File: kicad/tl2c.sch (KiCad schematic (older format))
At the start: 31 parts, among them IC101 ATTINY20-X, P101 12VDC, P102 I2C Master, P103 Spare, P104 ISP Header, P105 LED_DRIVER, P106 240VAC, P107 LED_DRIVER, P108 LED_OUT, SW101 TL3315NF160Q

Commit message: Revamped the master pcb layout for the mounting holes and the actual footprint for the terminal blocks
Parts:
- P102: footprint Pin_Headers:Pin_Header_Straight_1x03 -> tl2c-footprint:Spring_Terminal_Block_1_x_3
- P106: footprint tl2c-footprint:Pin_Header_1_x_2_5mmPitch -> tl2c-footprint:Spring_Terminal_Block_1_x_2_5mm
- P108: footprint tl2c-footprint:Pin_Header_1_x_6_54mmPitch -> tl2c-footprint:Spring_Terminal_Block_1_x_6_5mm; Conrad-PN (none) -> Value; Digikey-PN (none) -> Value; MFP (none) -> Value
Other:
- note added: "Should a PTC be considered?"
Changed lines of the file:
@@
 F 0 "P102" H 2100 3250 50  0000 C CNN
 F 1 "I2C Master" V 2200 3050 50  0000 C CNN
-F 2 "Pin_Headers:Pin_Header_Straight_1x03" H 2100 3050 50  0001 C CNN
+F 2 "tl2c-footprint:Spring_Terminal_Block_1_x_3" H 2100 3050 50  0001 C CNN
 F 3 "" H 2100 3050 50  0000 C CNN
 F 4 "Value" H 2100 3050 60  0001 C CNN "MFP"
@@
 F 0 "P106" H 6950 1350 50  0000 C CNN
 F 1 "240VAC" V 7050 1200 50  0000 C CNN
-F 2 "tl2c-footprint:Pin_Header_1_x_2_5mmPitch" H 6950 1200 50  0001 C CNN
+F 2 "tl2c-footprint:Spring_Terminal_Block_1_x_2_5mm" H 6950 1200 50  0001 C CNN
 F 3 "" H 6950 1200 50  0000 C CNN
 F 4 "Value" H 6950 1200 60  0001 C CNN "MFP"
@@
 F 0 "P108" H 9950 1750 50  0000 C CNN
 F 1 "LED_OUT" V 10050 1400 50  0000 C CNN
-F 2 "tl2c-footprint:Pin_Header_1_x_6_54mmPitch" H 9950 1400 50  0001 C CNN
+F 2 "tl2c-footprint:Spring_Terminal_Block_1_x_6_5mm" H 9950 1400 50  0001 C CNN
 F 3 "" H 9950 1400 50  0000 C CNN
+F 4 "Value" H 9950 1400 60  0001 C CNN "MFP"
+F 5 "Value" H 9950 1400 60  0001 C CNN "Conrad-PN"
+F 6 "Value" H 9950 1400 60  0001 C CNN "Digikey-PN"
 	1    9950 1400
 	1    0    0    -1
@@
 Text Notes 6850 4150 0    60   ~ 0
 TODO - Change the relay to  AZ7705T-1A-12DEF - Conrad.\nor FIN 43.41.7 12V - Reichelt
+Text Notes 6950 2450 0    60   ~ 0
+Should a PTC be considered?
 $EndSCHEMATC

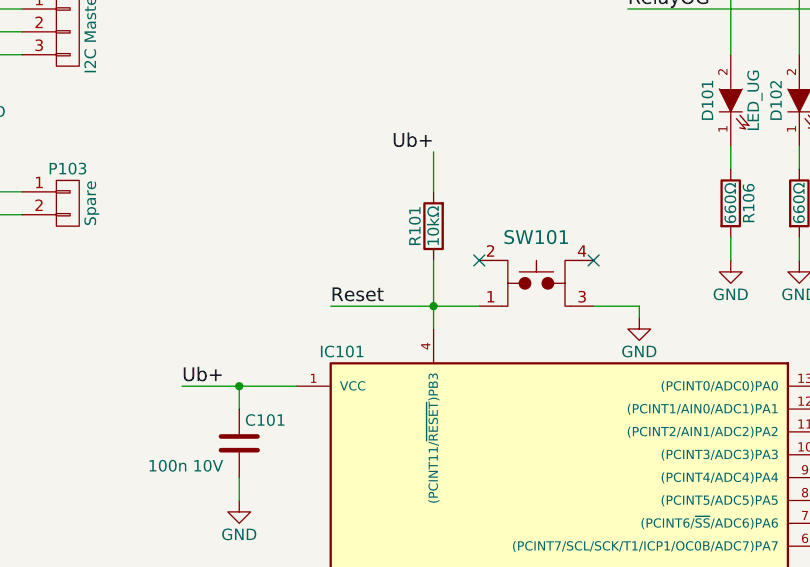
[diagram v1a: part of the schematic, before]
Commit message: Fixed junction on three wires instead of two, two wire connections. Added first look at the Gerbers
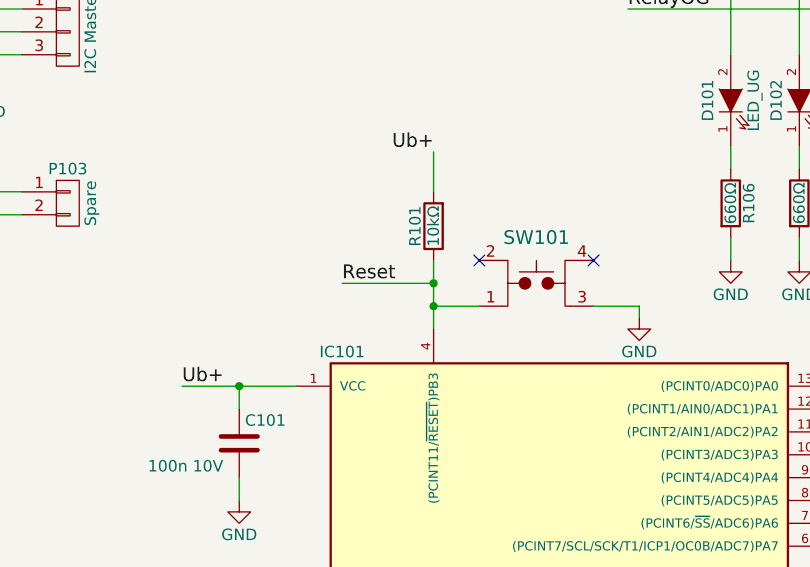
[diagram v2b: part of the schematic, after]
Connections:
- wire segments 97 -> 98
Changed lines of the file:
@@
 Wire Wire Line
 	3700 4050 3700 4350
-Wire Wire Line
-	3250 4250 3900 4250
-Connection ~ 3700 4250
-Text Label 3250 4250 0    60   ~ 0
+Text Label 3300 4150 0    60   ~ 0
 Reset
 NoConn ~ 3900 4050
@@
 Text Notes 6950 2450 0    60   ~ 0
 Should a PTC be considered?
+Wire Wire Line
+	3300 4150 3700 4150
+Connection ~ 3700 4150
+Wire Wire Line
+	3900 4250 3700 4250
+Connection ~ 3700 4250
 $EndSCHEMATC

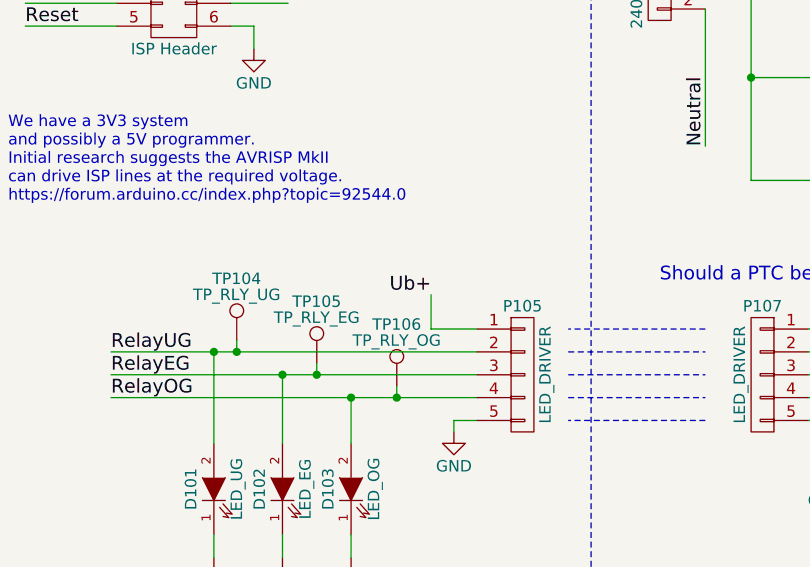
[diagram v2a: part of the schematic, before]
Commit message: Corrected the Ub+ to the LV board... should be U+
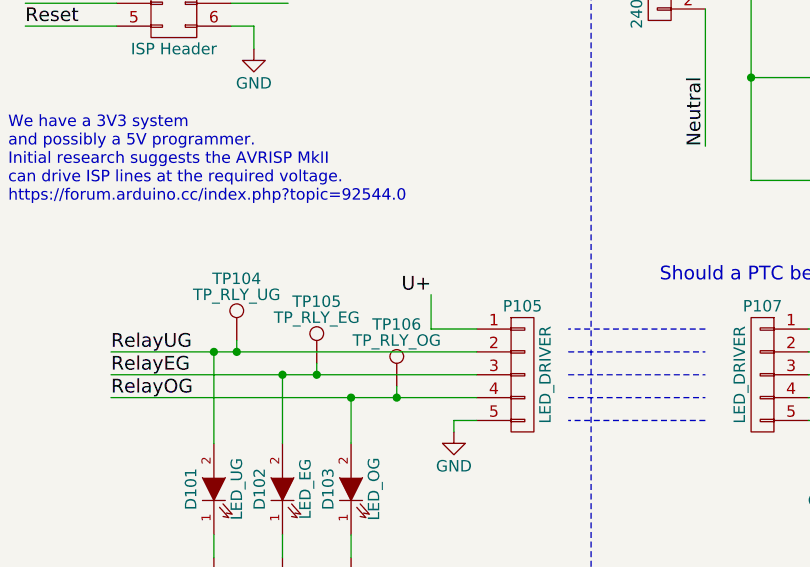
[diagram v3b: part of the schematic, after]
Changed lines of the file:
@@
 Wire Wire Line
 	5950 2650 5950 2500
-Text Label 5950 2500 2    60   ~ 0
-Ub+
 $Comp
 L CONN_01X05 P105
@@
 	3900 4250 3700 4250
 Connection ~ 3700 4250
+Text Label 5950 2500 2    60   ~ 0
+U+
 $EndSCHEMATC

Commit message: More rework on the board for the correct terminal blocks and case
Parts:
- removed P106: 240VAC, tl2c-footprint:Spring_Terminal_Block_1_x_2_5mm, symbol CONN_01X02
- removed P108: LED_OUT, tl2c-footprint:Spring_Terminal_Block_1_x_6_5mm, symbol CONN_01X06
- added P106: 240VAC, tl2c-footprint:Spring_Terminal_Block_1_x_2_5mm, symbol Term_01X02
- added P108: LED_OUT, tl2c-footprint:Spring_Terminal_Block_1_x_6_5mm, symbol TerminalBlock_1x6
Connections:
- wire segments 98 -> 107
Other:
- moved on the sheet: P107, REL101B, REL102B, REL103B

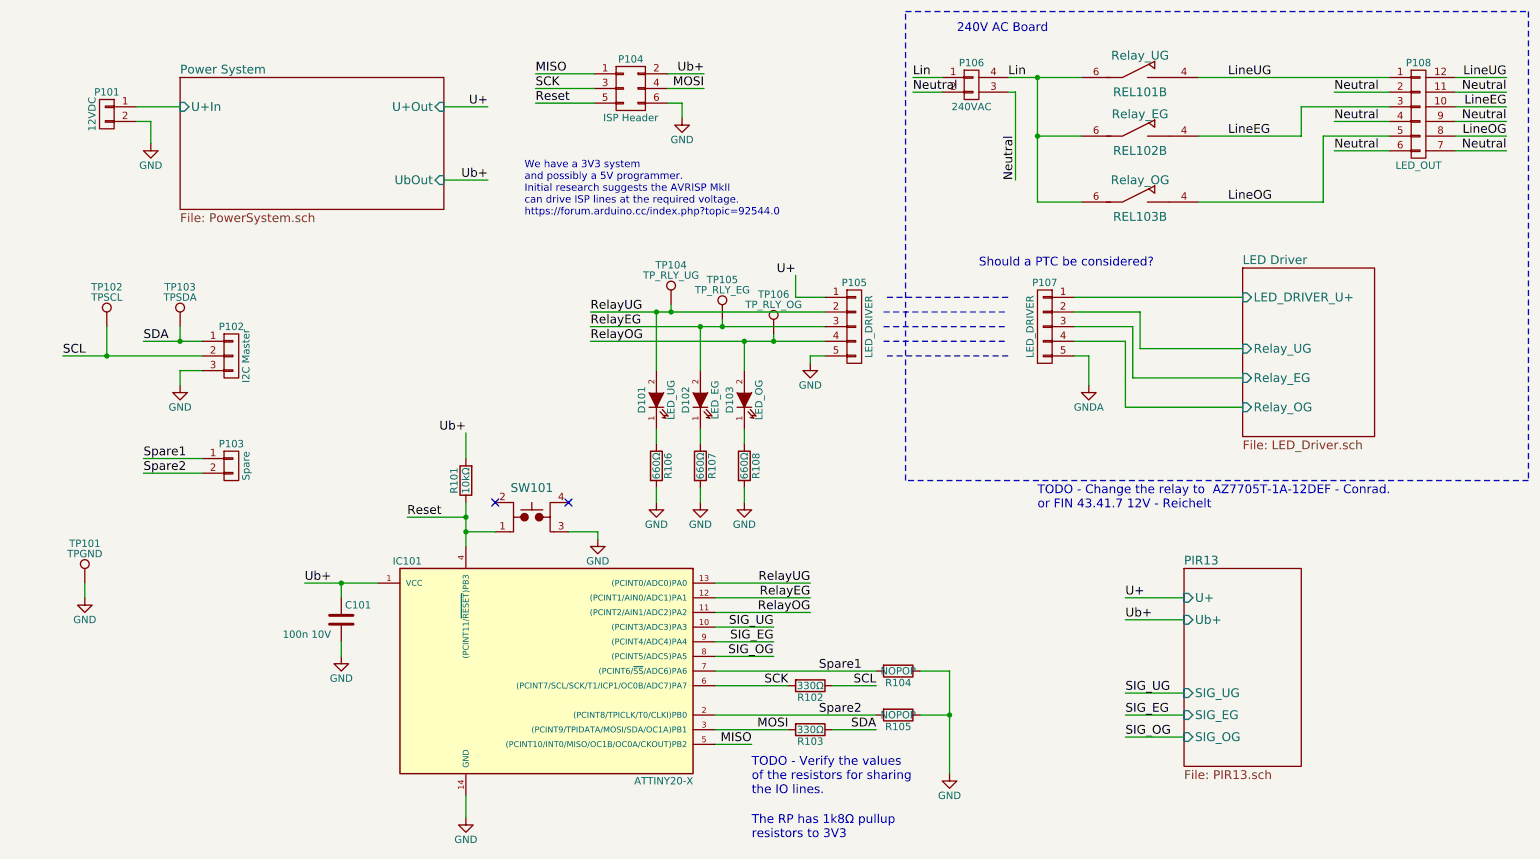
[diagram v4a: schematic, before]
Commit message: More layout re-work and footprint changes
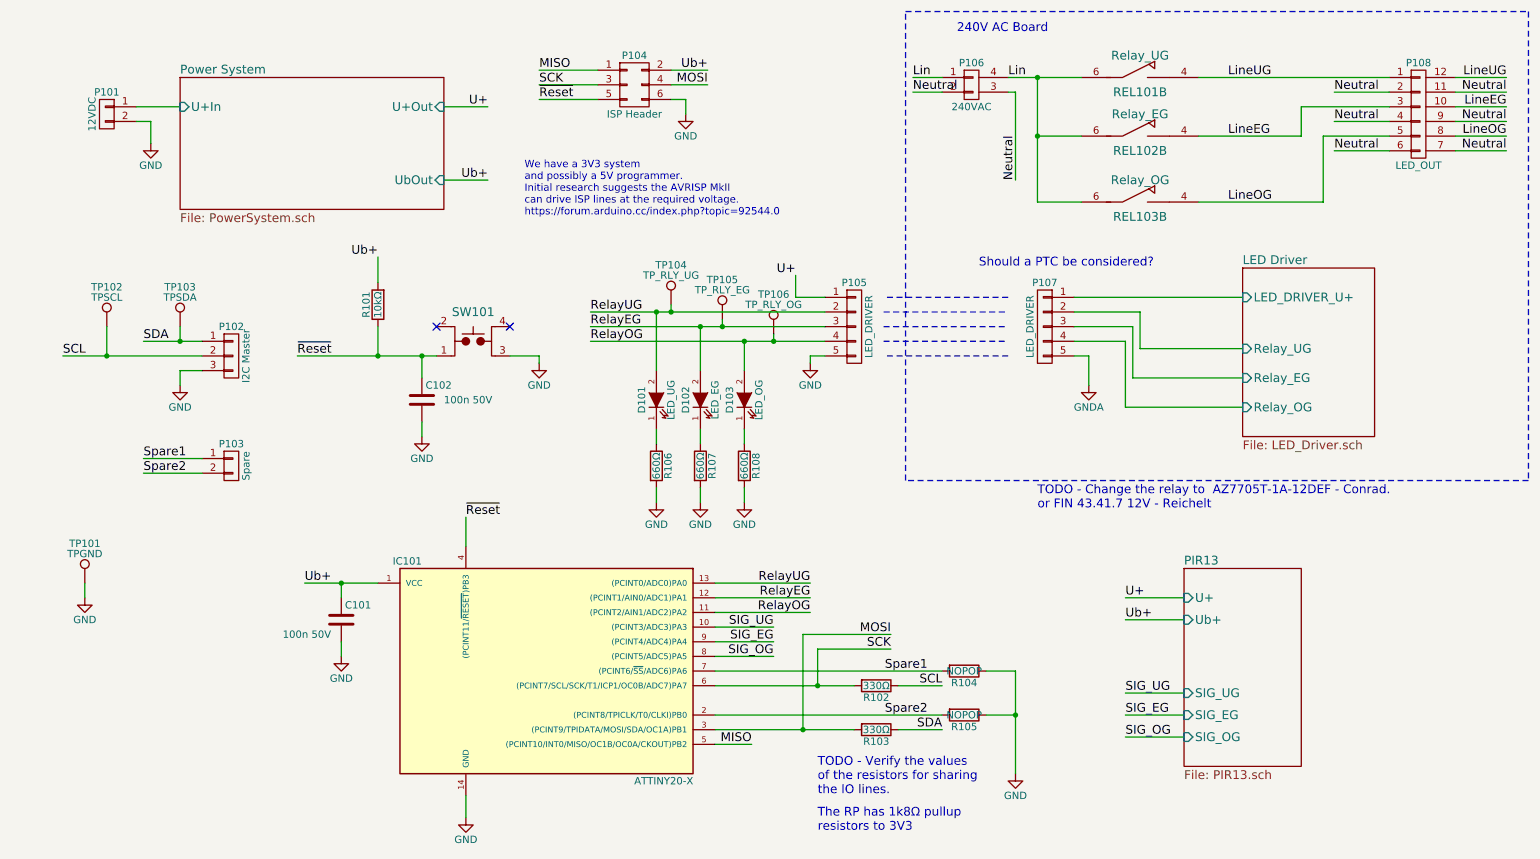
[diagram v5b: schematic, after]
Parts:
- added C102: 100n 50V, Capacitors_SMD:C_0805, symbol C
- C101: value 100n 10V -> 100n 50V
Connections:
- net GND: now also C102.2
- net Reset renamed ~Reset
- net ~Reset: now also C102.1
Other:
- moved on the sheet: P104, R101, R102, R103, R104, R105, SW101

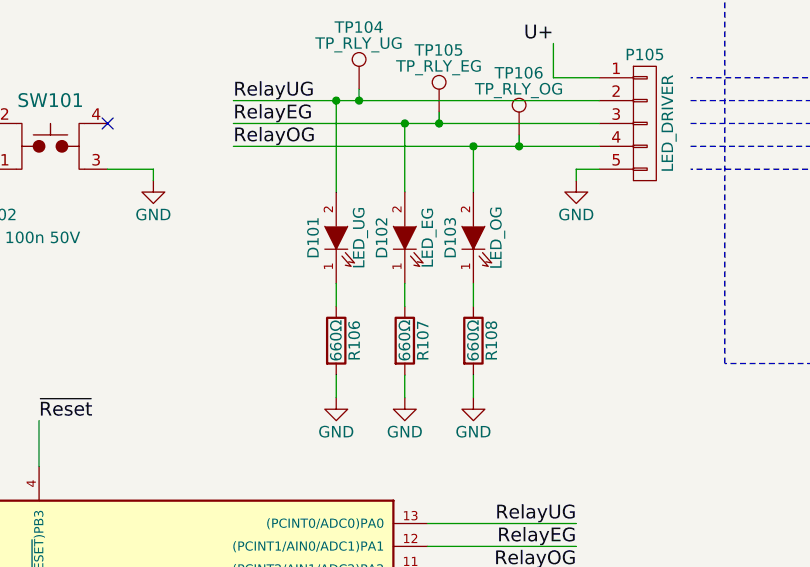
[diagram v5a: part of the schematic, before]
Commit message: Finished off the refactoring for the housing and terminal blocks
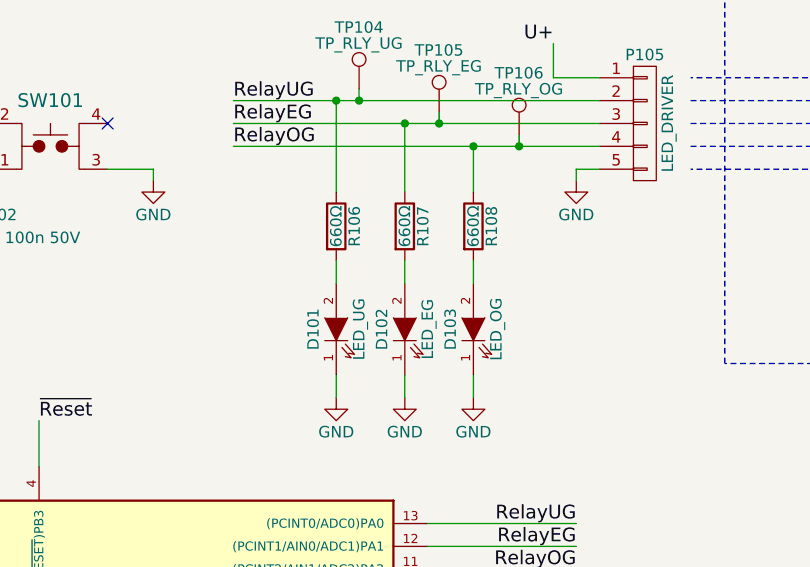
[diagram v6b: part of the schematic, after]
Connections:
- net GND: now also D101.1 (K), D102.1 (K), D103.1 (K); no longer R106.2, R107.2, R108.2
- net RelayEG: now also R107.1; no longer D102.2 (A)
- net RelayOG: now also R108.1; no longer D103.2 (A)
- net RelayUG: now also R106.1; no longer D101.2 (A)
- new net: D101.2 (A), R106.2
- new net: D102.2 (A), R107.2
- new net: D103.2 (A), R108.2
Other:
- moved on the sheet: D101, D102, D103, R106, R107, R108
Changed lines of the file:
@@
 L LED D101
 U 1 1 5856AA32
-P 5000 3350
-F 0 "D101" H 5000 3450 50  0000 C CNN
-F 1 "LED_UG" H 5000 3250 50  0000 C CNN
-F 2 "LEDs:LED_0805" H 5000 3350 50  0001 C CNN
-F 3 "" H 5000 3350 50  0000 C CNN
-	1    5000 3350
+P 5000 3750
+F 0 "D101" H 5000 3850 50  0000 C CNN
+F 1 "LED_UG" H 5000 3650 50  0000 C CNN
+F 2 "LEDs:LED_0805" H 5000 3750 50  0001 C CNN
+F 3 "" H 5000 3750 50  0000 C CNN
+	1    5000 3750
 	0    -1   -1   0
 $EndComp
@@
 L R R106
 U 1 1 5856AB2B
-P 5000 3800
-F 0 "R106" V 5080 3800 50  0000 C CNN
-F 1 "660Ω" V 5000 3800 50  0000 C CNN
-F 2 "Resistors_SMD:R_0805" V 4930 3800 50  0001 C CNN
-F 3 "" H 5000 3800 50  0000 C CNN
-	1    5000 3800
-	1    0    0    -1
-$EndComp
-Wire Wire Line
-	5000 3550 5000 3650
+P 5000 3300
+F 0 "R106" V 5080 3300 50  0000 C CNN
+F 1 "660Ω" V 5000 3300 50  0000 C CNN
+F 2 "Resistors_SMD:R_0805" V 4930 3300 50  0001 C CNN
+F 3 "" H 5000 3300 50  0000 C CNN
+	1    5000 3300
+	1    0    0    -1
+$EndComp
 $Comp
 L GND #PWR010
@@
 L LED D102
 U 1 1 5856B277
-P 5300 3350
-F 0 "D102" H 5300 3450 50  0000 C CNN
-F 1 "LED_EG" H 5300 3250 50  0000 C CNN
-F 2 "LEDs:LED_0805" H 5300 3350 50  0001 C CNN
-F 3 "" H 5300 3350 50  0000 C CNN
-	1    5300 3350
+P 5300 3750
+F 0 "D102" H 5300 3850 50  0000 C CNN
+F 1 "LED_EG" H 5300 3650 50  0000 C CNN
+F 2 "LEDs:LED_0805" H 5300 3750 50  0001 C CNN
+F 3 "" H 5300 3750 50  0000 C CNN
+	1    5300 3750
 	0    -1   -1   0
 $EndComp
@@
 L R R107
 U 1 1 5856B27D
-P 5300 3800
-F 0 "R107" V 5380 3800 50  0000 C CNN
-F 1 "660Ω" V 5300 3800 50  0000 C CNN
-F 2 "Resistors_SMD:R_0805" V 5230 3800 50  0001 C CNN
-F 3 "" H 5300 3800 50  0000 C CNN
-	1    5300 3800
-	1    0    0    -1
-$EndComp
-Wire Wire Line
-	5300 3550 5300 3650
+P 5300 3300
+F 0 "R107" V 5380 3300 50  0000 C CNN
+F 1 "660Ω" V 5300 3300 50  0000 C CNN
+F 2 "Resistors_SMD:R_0805" V 5230 3300 50  0001 C CNN
+F 3 "" H 5300 3300 50  0000 C CNN
+	1    5300 3300
+	1    0    0    -1
+$EndComp
 $Comp
 L GND #PWR011
@@
 L LED D103
 U 1 1 5856B503
-P 5600 3350
-F 0 "D103" H 5600 3450 50  0000 C CNN
-F 1 "LED_OG" H 5600 3250 50  0000 C CNN
-F 2 "LEDs:LED_0805" H 5600 3350 50  0001 C CNN
-F 3 "" H 5600 3350 50  0000 C CNN
-	1    5600 3350
+P 5600 3750
+F 0 "D103" H 5600 3850 50  0000 C CNN
+F 1 "LED_OG" H 5600 3650 50  0000 C CNN
+F 2 "LEDs:LED_0805" H 5600 3750 50  0001 C CNN
+F 3 "" H 5600 3750 50  0000 C CNN
+	1    5600 3750
 	0    -1   -1   0
 $EndComp
@@
 L R R108
 U 1 1 5856B509
-P 5600 3800
-F 0 "R108" V 5680 3800 50  0000 C CNN
-F 1 "660Ω" V 5600 3800 50  0000 C CNN
-F 2 "Resistors_SMD:R_0805" V 5530 3800 50  0001 C CNN
-F 3 "" H 5600 3800 50  0000 C CNN
-	1    5600 3800
-	1    0    0    -1
-$EndComp
-Wire Wire Line
-	5600 3550 5600 3650
+P 5600 3300
+F 0 "R108" V 5680 3300 50  0000 C CNN
+F 1 "660Ω" V 5600 3300 50  0000 C CNN
+F 2 "Resistors_SMD:R_0805" V 5530 3300 50  0001 C CNN
+F 3 "" H 5600 3300 50  0000 C CNN
+	1    5600 3300
+	1    0    0    -1
+$EndComp
 $Comp
 L GND #PWR012
@@
 	3100 2850 3100 3050
 Connection ~ 3100 3050
+Wire Wire Line
+	5000 3450 5000 3550
+Wire Wire Line
+	5300 3450 5300 3550
+Wire Wire Line
+	5600 3450 5600 3550
 $EndSCHEMATC
